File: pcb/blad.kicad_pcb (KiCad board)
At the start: 2 copper layers, 228.6 x 76.2 mm, 117 parts, among them J1 HRO_TYPE-C-31-M-12, J2 SWD, Q1 AO3401A, SW1 1U, SW10 1U, SW11 1U, SW12 1U, SW13 1.25U, SW14 1U, SW15 1U, SW16 1U, SW17 1U, SW18 1U, SW19 1U, SW2 1U, SW20 1U, SW21 1U, SW22 1U, SW23 1.75U, SW24 1.75U, SW25 1U, SW26 1U, SW27 1U, SW28 1U, SW29 1U, SW3 1U, SW30 1U, SW31 1U, SW32 1U, SW33 1U, SW34 1.25U, SW35 1.25U, SW36 1U, SW37 1.25U, SW38 2.75U, SW39 2.25U, SW4 1U, SW40 1.25U, SW41 1U, SW42 1.25U, SW5 1U, SW6 1U, SW7 1U, SW8 1U, SW9 1U, U1 SRV05-4, U2 MS88SF21 1Y40AI-U

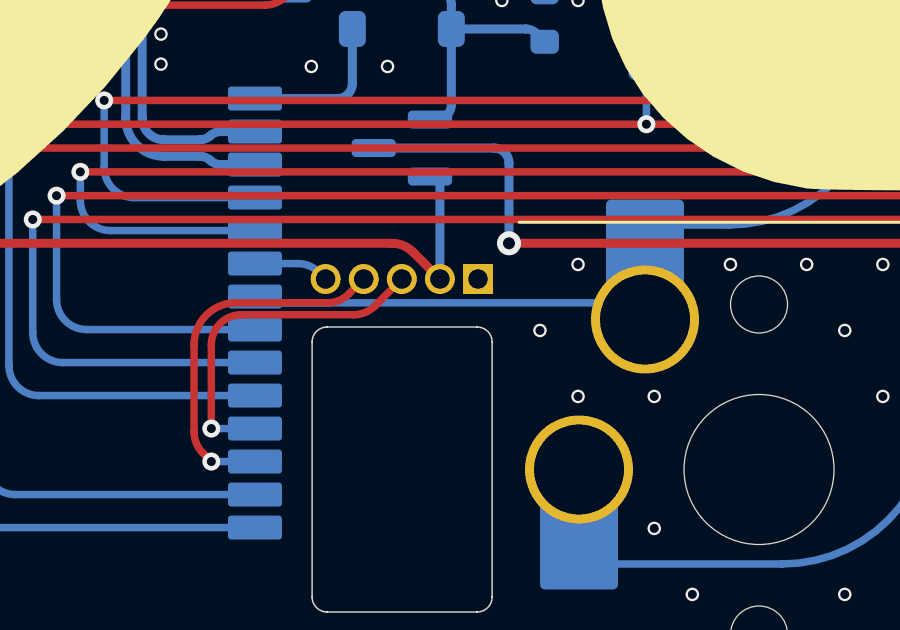
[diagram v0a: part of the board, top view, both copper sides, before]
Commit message: Update diode values and PCB data
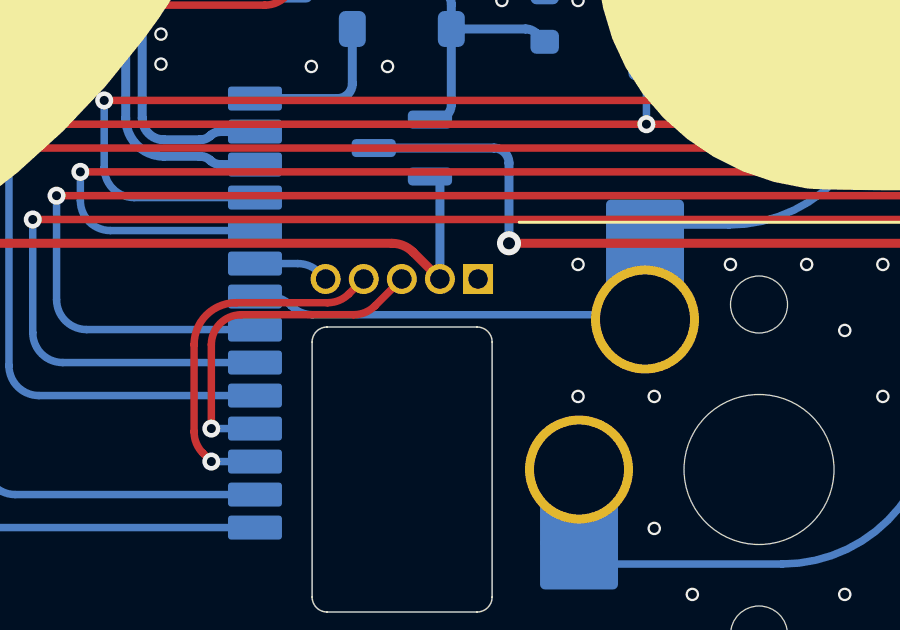
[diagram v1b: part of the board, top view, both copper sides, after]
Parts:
- D1, D10, D11, D12, D13, D14, D15, D16, D17, D18, D19, D2, D20, D21, D22, D23, D24, D25, D26, D27, D28, D29, D3, D30, D31, D32, D33, D34, D35, D36, D37, D38, D39, D4, D40, D41, D42, D5, D6, D7, D8, D9: value 1N4148WS -> 1N4148W
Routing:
- net GND: vias 1793 -> 1792

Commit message: Update keyboard design and renderings
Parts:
- moved S1 163.2 mm to (91.3, 171.4), turned to 90 degrees
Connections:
- S1 pad 1: GND -> unconnected-(S1-A-Pad1)
- S1 pad 3: unconnected-(S1-C-Pad3) -> GND
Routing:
- net Net-(BT1--): track 50.0 -> 131.9 mm
- net ROW4: track 140.4 -> 135.9 mm
- net COL3: track 275.7 -> 271.7 mm
- net ROW6: track 189.4 -> 186.8 mm
- net COL5: track 230.5 -> 228.1 mm
- net ROW1: track 315.1 -> 312.9 mm
- net GND: track 0.00 -> 1.48 mm, vias 1792 -> 1790
- net VDD: track 31.5 -> 30.2 mm
- net ROW3: track 284.0 -> 283.3 mm
- net ROW5: track 170.8 -> 170.2 mm
